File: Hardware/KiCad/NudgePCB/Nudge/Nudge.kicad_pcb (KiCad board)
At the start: 2 copper layers, 29 parts, among them J1 Conn_01x02, J2 Conn_01x03, J3 Conn_01x02, J4 Conn_01x02, J5 Conn_01x06, J6 Conn_01x06, SW1 SW_SPST, U1 XIAO-ESP32-S3-SMD

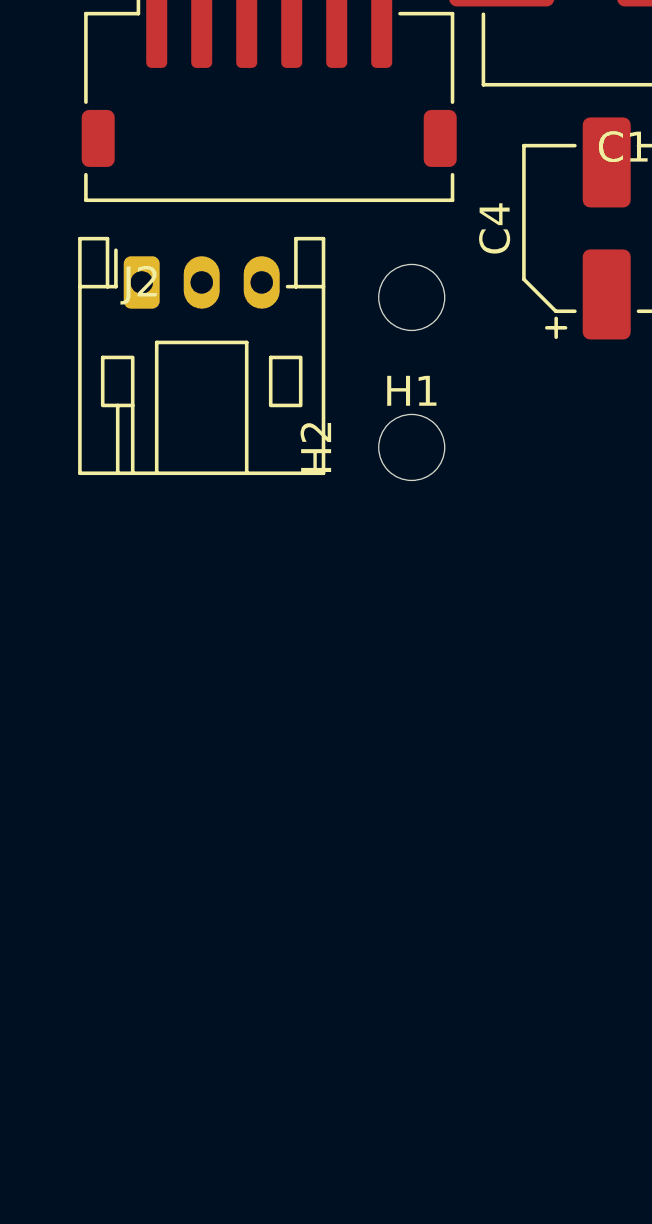
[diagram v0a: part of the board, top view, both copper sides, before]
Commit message: Main board PCB: 12-pin EMG strip header (J2) in sync with the schematic
Swaps the MyoWare JST footprint for a 1x12 2.54mm header at the same spot and
puts the strip's nets on the XIAO's D0 and bottom pads. The board is still an
unrouted placement draft (no outline, no tracks); schematic parity is back to
its original state (only the existing DRV8833 pin 15/16 note remains).

Co-Authored-By: Claude Opus 5.5 (1M context) <noreply@anthropic.com>
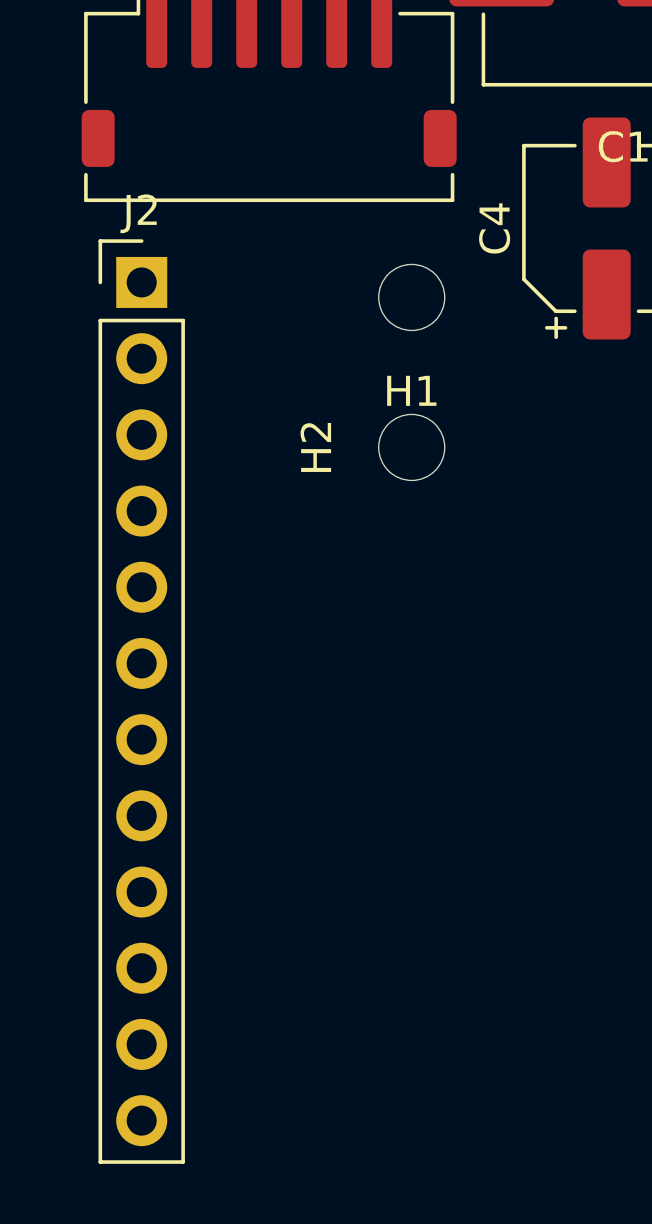
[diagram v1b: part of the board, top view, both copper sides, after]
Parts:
- J2: value Conn_01x03 -> EMG_Strip; footprint Connector_JST:JST_PH_S3B-PH-K_1x03_P2.00mm_Horizontal -> Connector_PinHeader_2.54mm:PinHeader_1x12_P2.54mm_Vertical
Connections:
- J2 pad 2: GND -> /STRIP_SCLK
- J2 pad 3: /EMG -> /STRIP_DIN
- U1 pad 1: /EMG -> /STRIP_DRDY
- U1 pad 15: unconnected-(U1-MTDI-Pad15) -> /STRIP_DOUT
- U1 pad 16: unconnected-(U1-MTDO-Pad16) -> /STRIP_DIN
- U1 pad 19: unconnected-(U1-MTMS-Pad19) -> /STRIP_CS
- U1 pad 20: unconnected-(U1-MTCK-Pad20) -> /STRIP_SCLK
